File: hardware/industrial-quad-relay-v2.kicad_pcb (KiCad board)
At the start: 2 copper layers, 40 x 40 mm, 36 parts, among them P1 CON-SENSOR, P2 Digital Output, P3 Debug, P4 Boot, U1 XMC1100, U2 CPC1020N, U3 CPC1020N, U4 CPC1020N, U5 CPC1020N, U6 DRILL, U7 DRILL, U8 DRILL, U9 DRILL

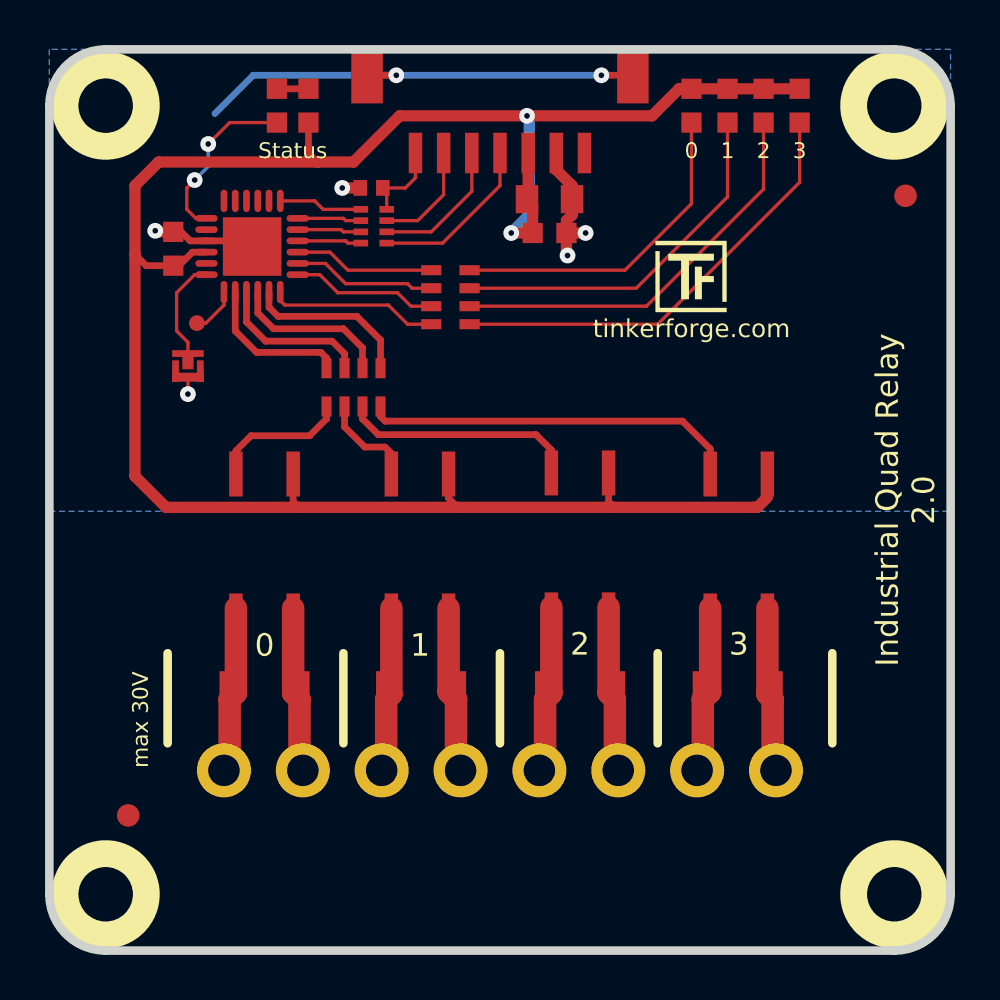
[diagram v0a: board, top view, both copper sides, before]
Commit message: add version 2.1
change CPC1020N -> CPC1002N
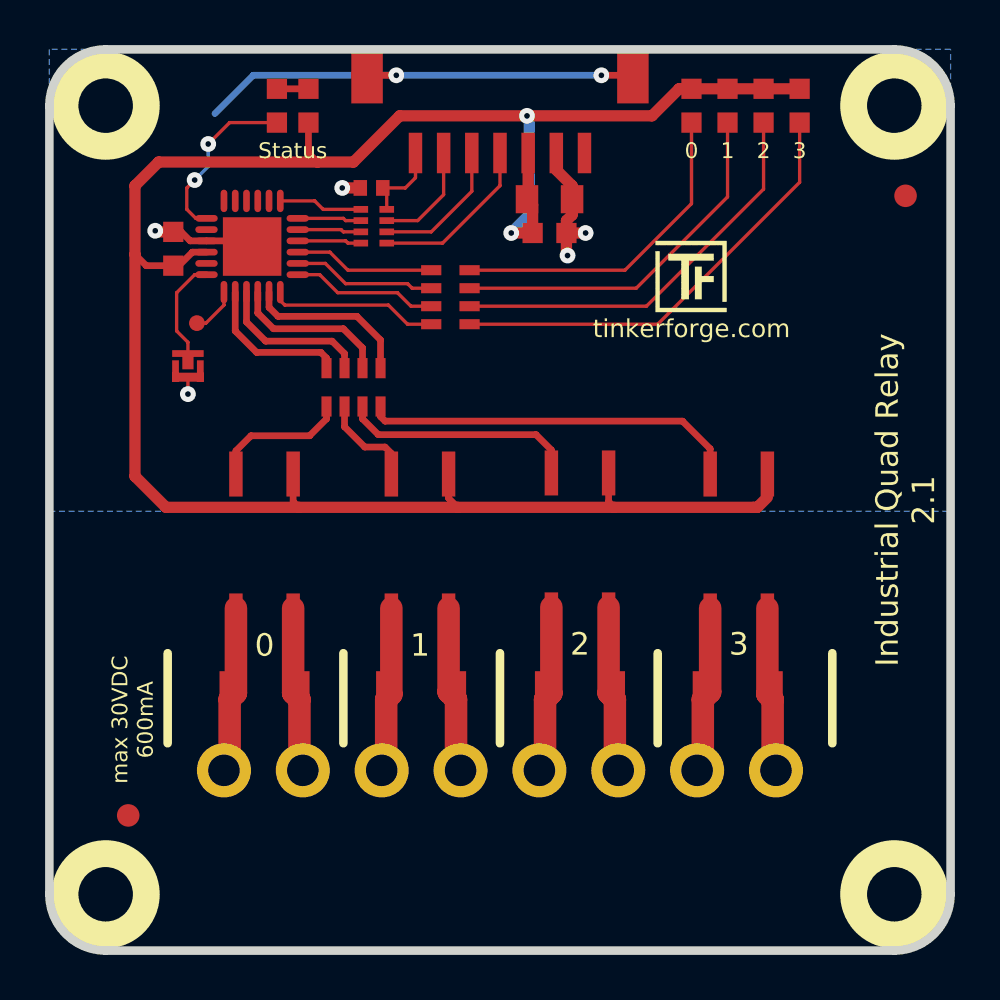
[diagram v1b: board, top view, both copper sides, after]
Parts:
- U2, U3, U4, U5: value CPC1020N -> CPC1002N
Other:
- board text added: "Copyright Tinkerforge GmbH 2021. This documentation describes Open Hardware and is licensed under the CERN OHL v. 1.1. You may redistribute and modify this documentation under the terms of the CERN OHL v.1.1. (http://ohwr.org/cernohl). This documentation is distributed WITHOUT ANY EXPRESS OR IMPLIED WARRANTY, INCLUDING OF MERCHANTABILITY, SATISFACTORY QUALITY AND FITNESS FOR A PARTICULAR PURPOSE.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"
- board text added: "Industrial Quad Relay 2.1"
- board text added: "max 30VDC 600mA"
- board text removed: "Copyright Tinkerforge GmbH 2018. This documentation describes Open Hardware and is licensed under the CERN OHL v. 1.1. You may redistribute and modify this documentation under the terms of the CERN OHL v.1.1. (http://ohwr.org/cernohl). This documentation is distributed WITHOUT ANY EXPRESS OR IMPLIED WARRANTY, INCLUDING OF MERCHANTABILITY, SATISFACTORY QUALITY AND FITNESS FOR A PARTICULAR PURPOSE.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"
- board text removed: "Industrial Quad Relay 2.0"
- board text removed: "max 30V"
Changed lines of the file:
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@@
-(kicad_pcb (version 20171130) (host pcbnew 5.0.1-33cea8e~67~ubuntu18.04.1)
+(kicad_pcb (version 20171130) (host pcbnew 5.1.12-84ad8e8a86~92~ubuntu20.04.1)
   (general
     (thickness 1.6002)
@@
   (title_block
     (title "Industrial Quad Relay Bricklet")
-    (date 2018-01-12)
-    (rev 2.0)
+    (date 2021-12-03)
+    (rev 2.1)
     (company "Tinkerforge GmbH")
     (comment 1 "Licensed under CERN OHL v.1.1")
-    (comment 2 "Copyright (©) 2018, B.Nordmeyer <bastian@tinkerforge.com>")
+    (comment 2 "Copyright (©) 2021, B.Nordmeyer <bastian@tinkerforge.com>")
   )
   (layers
     (0 Front signal)
-    (31 Back signal hide)
+    (31 Back signal)
     (32 B.Adhes user)
     (33 F.Adhes user)
@@
     (zone_45_only no)
     (trace_min 0.14986)
-    (segment_width 0.381)
-    (edge_width 0.381)
     (via_size 0.70104)
     (via_drill 0.24892)
@@
     (uvia_min_size 0.70104)
     (uvia_min_drill 0.24892)
+    (edge_width 0.381)
+    (segment_width 0.381)
     (pcb_text_width 0.3048)
     (pcb_text_size 1.524 2.032)
@@
       (effects (font (size 0.29972 0.29972) (thickness 0.07493)))
     )
-    (fp_text value CPC1020N (at 0 0) (layer F.Fab)
+    (fp_text value CPC1002N (at 0 0) (layer F.Fab)
       (effects (font (size 0.29972 0.29972) (thickness 0.07493)))
     )
@@
       (effects (font (size 0.29972 0.29972) (thickness 0.07493)))
     )
-    (fp_text value CPC1020N (at 0 0) (layer F.Fab)
+    (fp_text value CPC1002N (at 0 0) (layer F.Fab)
       (effects (font (size 0.29972 0.29972) (thickness 0.07493)))
     )
@@
       (effects (font (size 0.29972 0.29972) (thickness 0.07493)))
     )
-    (fp_text value CPC1020N (at 0 0) (layer F.Fab)
+    (fp_text value CPC1002N (at 0 0) (layer F.Fab)
       (effects (font (size 0.29972 0.29972) (thickness 0.07493)))
     )
@@
       (effects (font (size 0.29972 0.29972) (thickness 0.07493)))
     )
-    (fp_text value CPC1020N (at 0 0) (layer F.Fab)
+    (fp_text value CPC1002N (at 0 0) (layer F.Fab)
       (effects (font (size 0.29972 0.29972) (thickness 0.07493)))
     )
@@
     (effects (font (size 0.70104 0.70104) (thickness 0.14986)))
   )
-  (gr_text "Copyright Tinkerforge GmbH 2018.\nThis documentation describes Open Hardware and is licensed under the\nCERN OHL v. 1.1.\nYou may redistribute and modify this documentation under the terms of the\nCERN OHL v.1.1. (http://ohwr.org/cernohl). This documentation is distributed\nWITHOUT ANY EXPRESS OR IMPLIED WARRANTY, INCLUDING OF\nMERCHANTABILITY, SATISFACTORY QUALITY AND FITNESS FOR A\nPARTICULAR PURPOSE. Please see the CERN OHL v.1.1 for applicable\nconditions" (at 253.4 153.85) (layer Cmts.User)
+  (gr_text "Copyright Tinkerforge GmbH 2021.\nThis documentation describes Open Hardware and is licensed under the\nCERN OHL v. 1.1.\nYou may redistribute and modify this documentation under the terms of the\nCERN OHL v.1.1. (http://ohwr.org/cernohl). This documentation is distributed\nWITHOUT ANY EXPRESS OR IMPLIED WARRANTY, INCLUDING OF\nMERCHANTABILITY, SATISFACTORY QUALITY AND FITNESS FOR A\nPARTICULAR PURPOSE. Please see the CERN OHL v.1.1 for applicable\nconditions" (at 253.4 153.85) (layer Cmts.User)
     (effects (font (size 0.8001 0.8001) (thickness 0.200025)))
   )
-  (gr_text "max 30V" (at 101.84892 67.80022 90) (layer F.SilkS)
+  (gr_text "max 30VDC\n600mA" (at 101.5 67.80022 90) (layer F.SilkS)
     (effects (font (size 0.70104 0.70104) (thickness 0.14986)))
   )
@@
     (effects (font (size 1.00076 1.00076) (thickness 0.14986)))
   )
-  (gr_text "Industrial Quad Relay\n2.0" (at 135.8 58.05 90) (layer F.SilkS)
+  (gr_text "Industrial Quad Relay\n2.1" (at 135.8 58.05 90) (layer F.SilkS)
     (effects (font (size 1 1) (thickness 0.15)))
   )
@@
     (effects (font (size 0.8001 0.8001) (thickness 0.14986)))
   )
-  (gr_arc (start 100.29952 40.5511) (end 97.80016 40.5511) (angle 90) (layer Edge.Cuts) (width 0.381))
-  (gr_arc (start 100.29952 75.54976) (end 100.29952 78.04912) (angle 90) (layer Edge.Cuts) (width 0.381))
-  (gr_arc (start 135.29818 75.54976) (end 137.80008 75.54976) (angle 90) (layer Edge.Cuts) (width 0.381))
-  (gr_arc (start 135.29818 40.5511) (end 135.29818 38.0492) (angle 90) (layer Edge.Cuts) (width 0.381))
-  (gr_line (start 97.80016 40.5511) (end 97.80016 75.54976) (angle 90) (layer Edge.Cuts) (width 0.381))
-  (gr_line (start 135.30072 38.0492) (end 100.29952 38.0492) (angle 90) (layer Edge.Cuts) (width 0.381))
-  (gr_line (start 137.80262 75.54976) (end 137.80262 40.5511) (angle 90) (layer Edge.Cuts) (width 0.381))
-  (gr_line (start 100.29952 78.04912) (end 135.30072 78.04912) (angle 90) (layer Edge.Cuts) (width 0.381))
+  (gr_arc (start 100.3 40.55) (end 97.8 40.55) (angle 90) (layer Edge.Cuts) (width 0.381))
+  (gr_arc (start 100.3 75.55) (end 100.3 78.05) (angle 90) (layer Edge.Cuts) (width 0.381))
+  (gr_arc (start 135.3 75.55) (end 137.8 75.55) (angle 90) (layer Edge.Cuts) (width 0.381))
+  (gr_arc (start 135.3 40.55) (end 135.3 38.05) (angle 90) (layer Edge.Cuts) (width 0.381))
+  (gr_line (start 97.8 40.55) (end 97.8 75.55) (angle 90) (layer Edge.Cuts) (width 0.381))
+  (gr_line (start 135.3 38.05) (end 100.3 38.05) (angle 90) (layer Edge.Cuts) (width 0.381))
+  (gr_line (start 137.8 75.55) (end 137.8 40.55) (angle 90) (layer Edge.Cuts) (width 0.381))
+  (gr_line (start 100.3 78.05) (end 135.3 78.05) (angle 90) (layer Edge.Cuts) (width 0.381))
   (segment (start 126.3 39.8) (end 125.75 39.8) (width 0.50038) (layer Front) (net 1))
   (segment (start 119 41) (end 119 41) (width 0.50038) (layer Front) (net 1))

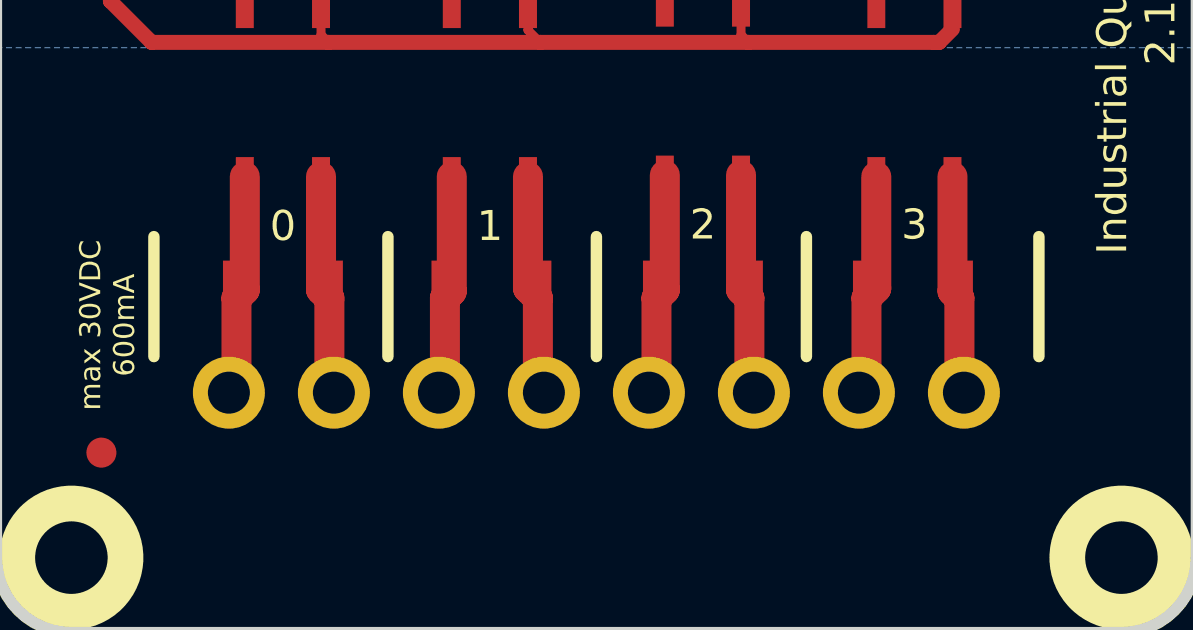
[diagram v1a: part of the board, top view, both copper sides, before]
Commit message: add silkscreen polarity markings
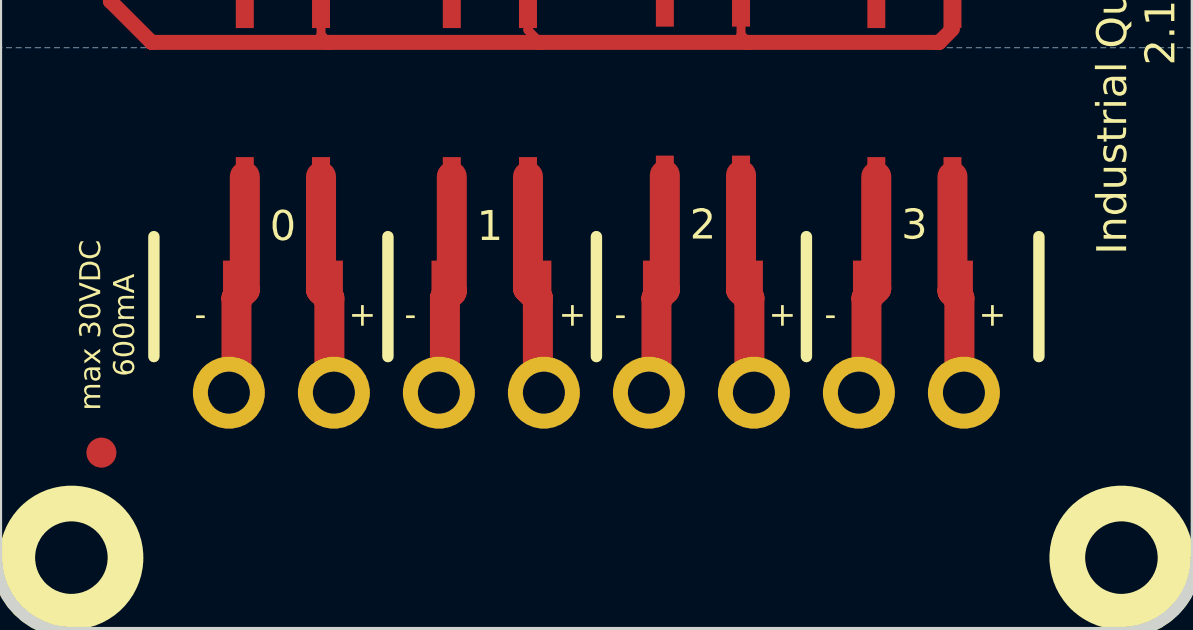
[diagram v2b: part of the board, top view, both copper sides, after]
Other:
- board text added: "+"
- board text added: "-"

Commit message: move to new kicad version
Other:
- net class Default removed
